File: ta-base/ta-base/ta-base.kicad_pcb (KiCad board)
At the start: 2 copper layers, 64 x 58 mm, 19 parts, among them J1 PinSocket_16_base, J2 PinSocket_4_base, J3 PinSocket_5_base, J4 PinSocket_4_base, J5 PinSocket_5_base, J6 PinSocket_16_base, J7 PinSocket_5_base, J8 PinSocket_5_base, P1 Gnd_Screws, P2 Gnd_standoffs, SW1 SW_SPDT, SW2 SW_SPDT, U1 TRANS_BSB008NE2LXXUMA1_INF, U2 burn_wire

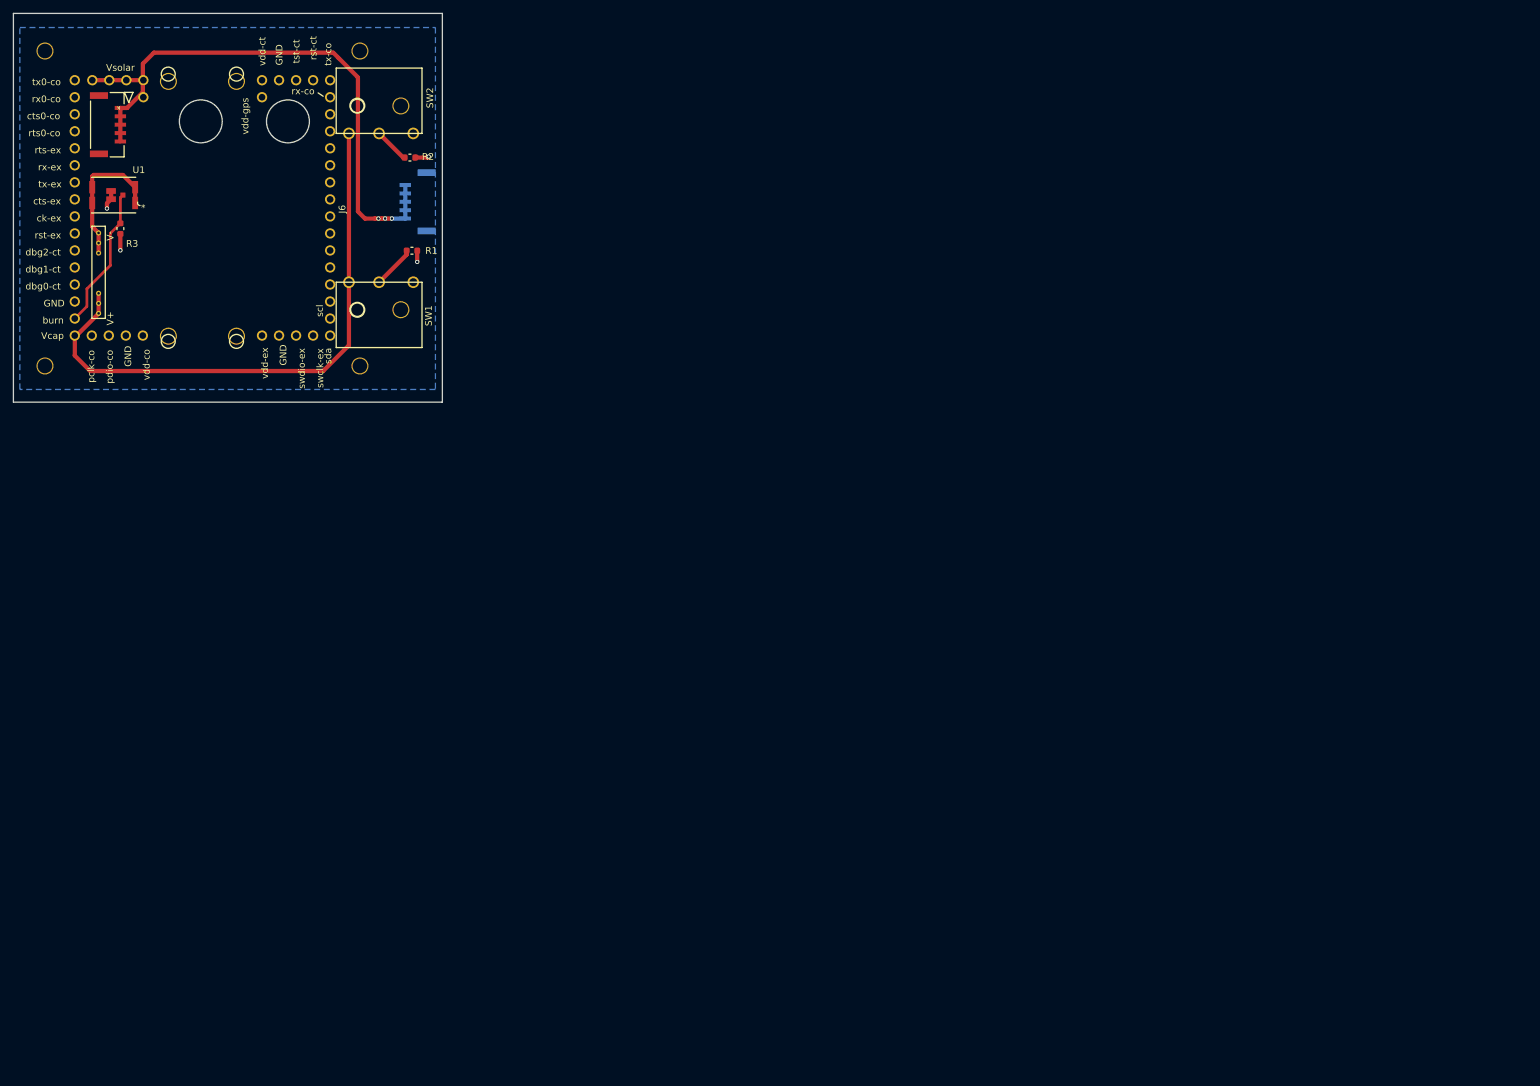
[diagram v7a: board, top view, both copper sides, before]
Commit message: finalized updates to base plate
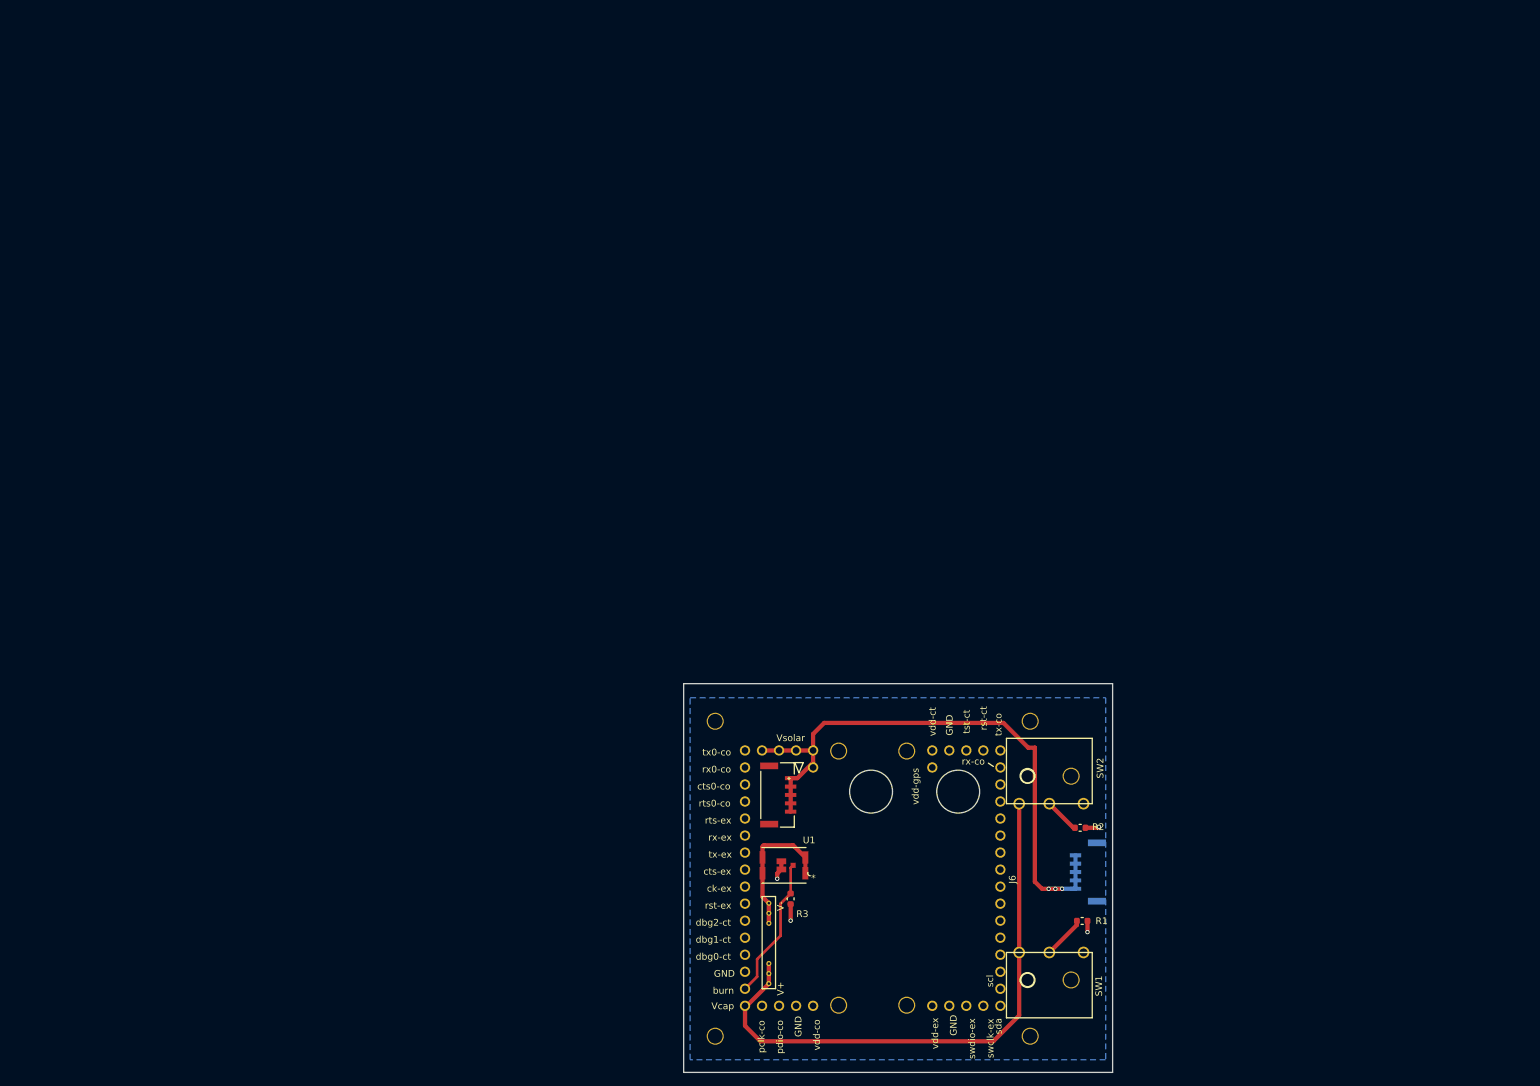
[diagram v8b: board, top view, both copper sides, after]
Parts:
- U1: value TRANS_BSB008NE2LXXUMA1_INF -> BSB008NE2LXXUMA1
- moved P2 170.3 mm to (123.1, 148.0), turned to 0 degrees
- moved J5 141.4 mm to (142.3, 110.0)
- moved J2 141.4 mm to (140.9, 148.1)
- moved J3 141.4 mm to (158.5, 125.6)
- moved J4 141.4 mm to (115.5, 148.1)
- moved J7 141.4 mm to (116.0, 114.1)
- moved P1 141.4 mm to (104.7, 152.6)
- moved R1 141.4 mm to (159.5, 135.4)
- moved R2 141.4 mm to (159.2, 121.5)
- moved R3 141.4 mm to (116.0, 132.1)
- moved REF** 141.4 mm to (128.0, 116.1)
- moved REF** 141.4 mm to (141.0, 116.1)
- moved SW1 141.4 mm to (154.6, 140.1)
- moved SW2 141.4 mm to (154.6, 117.9)
- moved U1 141.4 mm to (115.0, 127.1)
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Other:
- net class Default: clearance 0.1524 -> 0.3048
- rule trace_clearance: 0.1524 -> 0.3048
